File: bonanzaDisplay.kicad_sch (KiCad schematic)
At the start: 81 parts, among them J1 OLED-1.31-SSD1322, J15 SWD, J2 Conn_01x02, J5 Conn_01x10, J6 USB_C_Receptacle_USB2.0, SW1 TS-1088-AR02016, SW2 TS-1088-AR02016, SW3 SIQ-02FVS3, U1 RP2354A, U2 XC6206P302MR, U3 XC6206P282MR, U4 TPS62933DRLR, Y1 ABM8-272-T3

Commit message: updated version to v3. switch to 12P FPC
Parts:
- J5: footprint bonanzaDisplay:FPC-SMD_10P-P1.0_FGS-XJ-H2.0 -> bonanzaDisplay:FPC-SMD_12P-P1.00_FGS-XJ-H2.0; symbol bonanzaDisplay:FPC-SMD_10P-P1.0_FGS-XJ-H2.0 -> bonanzaDisplay:FPC-SMD_12P-P1.0_FGS-XJ-H2.0; LCSC C262756 -> C262757; PARTNO AFA01-S10FCA-00 -> AFA01-S12FCA-00
- TP22: value SCL -> TX
- TP23: value SDA -> RX
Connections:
- net GND: now also J5.13; no longer J5.11, J5.12
- net SWCLK: now also J5.12 (Pin_10)
- net DISP_SCL renamed DISP_TX
- net DISP_SDA renamed DISP_RX
- new net SWD-DISP: J5.11 (Pin_10)
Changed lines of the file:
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@@
 	(title_block
 		(title "bonanzaDisplay")
-		(date "2026-05-05")
-		(rev "v2")
+		(date "2026-10-01")
+		(rev "v3")
 		(company "bitaxeorg")
 		(comment 1 "OHL v2")
@@
 	(wire
 		(pts
+			(xy 71.12 134.62) (xy 57.15 134.62)
+		)
+		(stroke
+			(width 0)
+			(type default)
+		)
+	)
+	(wire
+		(pts
 			(xy 104.14 46.99) (xy 101.6 46.99)
 		)
@@
 	(wire
 		(pts
+			(xy 71.12 137.16) (xy 57.15 137.16)
+		)
+		(stroke
+			(width 0)
+			(type default)
+		)
+	)
+	(wire
+		(pts
 			(xy 218.44 58.42) (xy 223.52 58.42)
 		)
@@
 		)
 	)
+	(label "SWD-DISP"
+		(at 71.12 134.62 180)
+		(effects
+			(font
+				(size 1.27 1.27)
+			)
+			(justify right bottom)
+		)
+	)
 	(label "GND"
 		(at 256.54 227.33 0)
@@
 		)
 	)
+	(label "DISP_TX"
+		(at 71.12 127 180)
+		(effects
+			(font
+				(size 1.27 1.27)
+			)
+			(justify right bottom)
+		)
+	)
 	(label "SW_CCW"
 		(at 134.62 224.79 0)
@@
 		)
 	)
-	(label "DISP_SDA"
-		(at 247.65 144.78 180)
-		(effects
-			(font
-				(size 1.27 1.27)
-			)
-			(justify right bottom)
-		)
-	)
 	(label "GND"
 		(at 71.12 116.84 180)
@@
 		)
 	)
+	(label "DISP_RX"
+		(at 71.12 129.54 180)
+		(effects
+			(font
+				(size 1.27 1.27)
+			)
+			(justify right bottom)
+		)
+	)
 	(label "3V0"
 		(at 267.97 215.9 180)
@@
 		)
 	)
-	(label "DISP_SCL"
-		(at 71.12 127 180)
+	(label "DISP_RX"
+		(at 247.65 144.78 180)
+		(effects
+			(font
+				(size 1.27 1.27)
+			)
+			(justify right bottom)
+		)
+	)
+	(label "DISP_TX"
+		(at 247.65 147.32 180)
 		(effects
 			(font
@@
 		)
 	)
+	(label "SWCLK"
+		(at 71.12 137.16 180)
+		(effects
+			(font
+				(size 1.27 1.27)
+			)
+			(justify right bottom)
+		)
+	)
 	(label "E{slash}RD"
 		(at 320.04 170.18 0)
@@
 		)
 	)
-	(label "DISP_SCL"
-		(at 247.65 147.32 180)
-		(effects
-			(font
-				(size 1.27 1.27)
-			)
-			(justify right bottom)
-		)
-	)
 	(label "D1"
 		(at 320.04 165.1 0)
@@
 		)
 	)
-	(label "DISP_SDA"
-		(at 71.12 129.54 180)
-		(effects
-			(font
-				(size 1.27 1.27)
-			)
-			(justify right bottom)
-		)
-	)
 	(label "DISP_GPIO2"
 		(at 247.65 152.4 180)
@@
 			)
 		)
-		(property "Value" "SCL"
+		(property "Value" "TX"
 			(at 251.968 149.606 90)
 			(show_name no)
@@
 			)
 		)
-		(property "Value" "SDA"
+		(property "Value" "RX"
 			(at 263.398 147.066 90)
 			(show_name no)
@@
 	)
 	(symbol
-		(lib_id "bonanzaDisplay:FPC-SMD_10P-P1.0_FGS-XJ-H2.0")
+		(lib_id "bonanzaDisplay:FPC-SMD_12P-P1.0_FGS-XJ-H2.0")
 		(at 52.07 119.38 0)
 		(mirror y)
@@
 		(dnp no)
 		(property "Reference" "J5"
-			(at 52.07 134.874 0)
+			(at 52.07 106.68 0)
 			(show_name no)
 			(do_not_autoplace no)
@@
 		)
 		(property "Value" "Conn_01x10"
-			(at 51.816 136.652 0)
+			(at 51.816 139.954 0)
 			(show_name no)
 			(do_not_autoplace no)
@@
 			)
 		)
-		(property "Footprint" "bonanzaDisplay:FPC-SMD_10P-P1.0_FGS-XJ-H2.0"
-			(at 52.07 119.38 0)
+		(property "Footprint" "bonanzaDisplay:FPC-SMD_12P-P1.00_FGS-XJ-H2.0"
+			(at 52.07 143.002 0)
 			(hide yes)
 			(show_name no)
@@
 		)
 		(property "Datasheet" "https://www.lcsc.com/datasheet/C262756.pdf"
-			(at 52.07 119.38 0)
+			(at 52.07 143.002 0)
 			(hide yes)
 			(show_name no)
@@
 			)
 		)
-		(property "PARTNO" "AFA01-S10FCA-00"
-			(at 52.07 119.38 0)
+		(property "PARTNO" "AFA01-S12FCA-00"
+			(at 52.07 143.002 0)
 			(hide yes)
 			(show_name no)
@@
 			)
 		)
-		(property "LCSC" "C262756"
-			(at 52.07 119.38 0)
+		(property "LCSC" "C262757"
+			(at 51.562 145.034 0)
 			(hide yes)
 			(show_name no)
@@
 		(pin "11"
 		)
+		(pin "13"
+		)
+		(pin "14"
+		)
 		(instances

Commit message: rough placements and critical routing done
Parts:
- removed J6: USB_C_Receptacle_USB2.0, bonanzaDisplay:USB_C_Receptacle_GCT_USB4105-xx-A, symbol bonanzaDisplay:USB_C_Receptacle_USB2.0
- added J6: TYPE-C-31-M-12, bonanzaDisplay:USB-C_SMD-TYPE-C-31-M-12_1, symbol bitaxe:TYPE-C-31-M-12
- added TP64: VBUS, bonanzaDisplay:TestPoint_Pad_D1.0mm, symbol Connector:TestPoint
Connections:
- net SWD-DISP is gone; now on net SWD: J5.11 (Pin_10)
- net GND: now also J6.1 (SHIELD), J6.2 (EH), J6.3 (EH), J6.4 (EH), J6.A1B12 (GND), J6.B1A12 (GND)
- net USB_DN: now also J6.A7 (DN1), J6.B7 (DN2)
- net USB_DP: now also J6.A6 (DP1), J6.B6 (DP2)
- net at R4.2: now also J6.B5 (CC2)
- net at R2.2: now also J6.A5 (CC1)
- new net: J6.A4B9 (VBUS), J6.B4A9 (VBUS), TP64.1
- no-connect marks 21 -> 20
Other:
- moved on the sheet: R2, R4

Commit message: finished routing, DRC and ERC pass
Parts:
- removed H1, H2, H3, H4: MountingHole_Pad, MountingHole:MountingHole_3.2mm_M3, symbol Mechanical:MountingHole
- J6: symbol bitaxe:TYPE-C-31-M-12 -> bonanzaDisplay:TYPE-C-31-M-12
- SW1, SW2: symbol bitaxe:GT-TC029B-H025-L1N -> bonanzaDisplay:GT-TC029B-H025-L1N
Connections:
- net GND: now also J5.14
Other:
- note added: "Display Ref Voltage Regulators"
- moved on the sheet: C38, C39, C40, TP15, TP16, TP18, U2, U3

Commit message: add jlcpcb offsets
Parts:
- J1: FT Position Offset (none) -> 0,-3.4
- U2, U3, U4: FT Rotation Offset (none) -> -180
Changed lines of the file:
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@@
 			)
 		)
+		(property "FT Rotation Offset" "-180"
+			(at 241.3 219.71 0)
+			(hide yes)
+			(show_name no)
+			(do_not_autoplace no)
+			(effects
+				(font
+					(size 1.27 1.27)
+				)
+			)
+		)
 		(pin "3"
 		)
@@
 			)
 		)
+		(property "FT Rotation Offset" "-180"
+			(at 78.74 49.53 0)
+			(hide yes)
+			(show_name no)
+			(do_not_autoplace no)
+			(effects
+				(font
+					(size 1.27 1.27)
+				)
+			)
+		)
 		(pin "4"
 		)
@@
 			)
 		)
+		(property "FT Rotation Offset" "-180"
+			(at 241.3 243.84 0)
+			(hide yes)
+			(show_name no)
+			(do_not_autoplace no)
+			(effects
+				(font
+					(size 1.27 1.27)
+				)
+			)
+		)
 		(pin "3"
 		)
@@
 			(at 336.55 172.72 0)
 			(hide yes)
+			(show_name no)
+			(do_not_autoplace no)
+			(effects
+				(font
+					(size 1.27 1.27)
+				)
+			)
+		)
+		(property "FT Position Offset" "0,-3.4"
+			(at 336.55 172.72 0)
+			(hide yes)

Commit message: removed the OLED accessory voltage regulators -- we should be good with 3.3V. addressed VCOMH bypass cap voltage rating.
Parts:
- removed C38, C39, C40: 1uF, Capacitor_SMD:C_0402_1005Metric, symbol Device:C_Small
- removed R39: 4.7k, Resistor_SMD:R_0402_1005Metric, symbol Device:R_Small_US
- removed TP15: 3V0, bonanzaDisplay:TestPoint_Pad_D1.0mm, symbol Connector:TestPoint
- removed TP16: 2V8, bonanzaDisplay:TestPoint_Pad_D1.0mm, symbol Connector:TestPoint
- removed TP17: 1V1, bonanzaDisplay:TestPoint_Pad_D1.0mm, symbol Connector:TestPoint
- removed TP18: GND, bonanzaDisplay:TestPoint_Pad_D1.0mm, symbol Connector:TestPoint
- removed U2: XC6206P302MR, Package_TO_SOT_SMD:SOT-23, symbol bonanzaDisplay:XC6206
- removed U3: XC6206P282MR, Package_TO_SOT_SMD:SOT-23, symbol bonanzaDisplay:XC6206
- C26: footprint Capacitor_SMD:C_0402_1005Metric -> Capacitor_SMD:C_1206_3216Metric; Dielectric (none) -> X7R; LCSC C23733 -> C51205; Manufacturer Murata Electronics -> Samsung Electro-Mechanics; PARTNO CL05A475KP5NRNC -> CL31B475KBHNNNE; Tolerance (none) -> ±10%; Voltage (none) -> 50V
- J1: value OLED-1.31-SSD1322 -> OLED-3.12-SSD1322
- U1: private KLC_S4.2_VREG_LX -> KLC_S4.2_DVDD; private_1 (none) -> KLC_S4.2_VREG_LX
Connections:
- net 2V8 is gone; now on net 3V3: J1.24 (VDDIO)
- net 3V0 is gone; now on net 3V3: C19.1, C21.1, J1.17 (BS1)
- net 3V3: now also J1.26 (VCI)
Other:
- note added: "EA W256064-XALG 3.12" OLED Module"
- note added: "OLED logic supply: shared MCU 3V3 VCI, VDDIO and BS1 use the same rail. VDD (pin 25): internal regulator; C22 only."
- note removed: "Display Ref Voltage Regulators"

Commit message: Correct RP2354A crystal BOM and load capacitors (H3)
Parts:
- C16, C17: value 10pF -> 15pF; Dielectric (none) -> C0G; LCSC C32949 -> C1548; Manufacturer Murata Electronics -> FH (Guangdong Fenghua Advanced Tech); PARTNO (none) -> 0402CG150J500NT; Tolerance (none) -> ±5%; Voltage (none) -> 50V
- Y1: LCSC C9002 -> C20625731; Manufacturer Abracon -> Abracon LLC
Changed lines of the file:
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@@
 			)
 		)
-		(property "Datasheet" ""
+		(property "Datasheet" "https://abracon.com/datasheets/ABM8-272-T3.pdf"
 			(at 140.97 152.4 0)
 			(hide yes)
@@
 			)
 		)
-		(property "Manufacturer" "Abracon "
+		(property "Manufacturer" "Abracon LLC"
 			(at 140.97 152.4 0)
 			(hide yes)
@@
 			)
 		)
-		(property "LCSC" "C9002"
+		(property "LCSC" "C20625731"
 			(at 74.93 139.7 0)
 			(hide yes)
@@
 			)
 		)
-		(property "Value" "10pF"
+		(property "Value" "15pF"
 			(at 129.54 159.258 90)
 			(show_name no)
@@
 			)
 		)
-		(property "Datasheet" ""
+		(property "Datasheet" "https://www.lcsc.com/datasheet/lcsc_datasheet_2304140030_FH--Guangdong-Fenghua-Advanced-Tech-0402CG150J500NT_C1548.pdf"
 			(at 135.89 157.48 0)
 			(hide yes)
@@
 			)
 		)
-		(property "Manufacturer" "Murata Electronics"
+		(property "Manufacturer" "FH (Guangdong Fenghua Advanced Tech)"
 			(at 135.89 157.48 0)
 			(hide yes)
@@
 			)
 		)
-		(property "LCSC" "C32949"
+		(property "LCSC" "C1548"
 			(at 135.89 157.48 0)
 			(hide yes)
@@
 			)
 		)
-		(property "PARTNO" ""
+		(property "PARTNO" "0402CG150J500NT"
 			(at 135.89 157.48 90)
 			(hide yes)
@@
 			)
 		)
-	)
+		(property "Dielectric" "C0G"
+			(at 135.89 157.48 0)
+			(hide yes)
+			(effects
+				(font
+					(size 1.27 1.27)
+				)
+			)
+		)
+		(property "Tolerance" "±5%"
+			(at 135.89 157.48 0)
+			(hide yes)
+			(effects
+				(font
+					(size 1.27 1.27)
+				)
+			)
+		)
+		(property "Voltage" "50V"
+			(at 135.89 157.48 0)
+			(hide yes)
+			(effects
+				(font
+					(size 1.27 1.27)
+				)
+			)
+		))
 	(symbol
 		(lib_id "Device:R_Small_US")
@@
 			)
 		)
-		(property "Value" "10pF"
+		(property "Value" "15pF"
 			(at 129.794 148.59 90)
 			(show_name no)
@@
 			)
 		)
-		(property "Datasheet" ""
+		(property "Datasheet" "https://www.lcsc.com/datasheet/lcsc_datasheet_2304140030_FH--Guangdong-Fenghua-Advanced-Tech-0402CG150J500NT_C1548.pdf"
 			(at 135.89 147.32 0)
 			(hide yes)
@@
 			)
 		)
-		(property "Manufacturer" "Murata Electronics"
+		(property "Manufacturer" "FH (Guangdong Fenghua Advanced Tech)"
 			(at 135.89 147.32 0)
 			(hide yes)
@@
 			)
 		)
-		(property "LCSC" "C32949"
+		(property "LCSC" "C1548"
 			(at 135.89 147.32 0)
 			(hide yes)
@@
 			)
 		)
-		(property "PARTNO" ""
+		(property "PARTNO" "0402CG150J500NT"
 			(at 135.89 147.32 90)
 			(hide yes)
@@
 			)
 		)
-	)
+		(property "Dielectric" "C0G"
+			(at 135.89 147.32 0)
+			(hide yes)
+			(effects
+				(font
+					(size 1.27 1.27)
+				)
+			)
+		)
+		(property "Tolerance" "±5%"
+			(at 135.89 147.32 0)
+			(hide yes)
+			(effects
+				(font
+					(size 1.27 1.27)
+				)
+			)
+		)
+		(property "Voltage" "50V"
+			(at 135.89 147.32 0)
+			(hide yes)
+			(effects
+				(font
+					(size 1.27 1.27)
+				)
+			)
+		))
 	(symbol
 		(lib_id "bonanzaDisplay:FPC-SMD_12P-P1.0_FGS-XJ-H2.0")

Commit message: Sync reviewed v3.1 PCB fixes and protect BOOT chip-select
Add R40 (1k, 0402, C11702) between QSPI_SS and SW2, including the
reviewed via placement on its switch-side pad and refreshed zone fills.

Include the manually synchronized OLED power, bypass capacitor and
crystal changes, corrected C16/C17 MPNs, connector datasheet links,
and the v3.1 project revision metadata.

Validation: zero DRC violations, zero unconnected items, and zero
schematic/PCB parity mismatches. All 19 existing ERC findings are
unchanged. Hardware BOOTSEL testing and assembly-process checks remain
open.

Refs #3, #4, #5, #6, #8, #9, #12, #16
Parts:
- added R40: 1k, Resistor_SMD:R_0402_1005Metric, symbol Device:R_Small_US
- J5: value Conn_01x10 -> Conn_01x12
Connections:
- net at SW2.1: now also R40.2; no longer U1.60 (~{QSPI_SS})
- new net: R40.1, U1.60 (~{QSPI_SS})

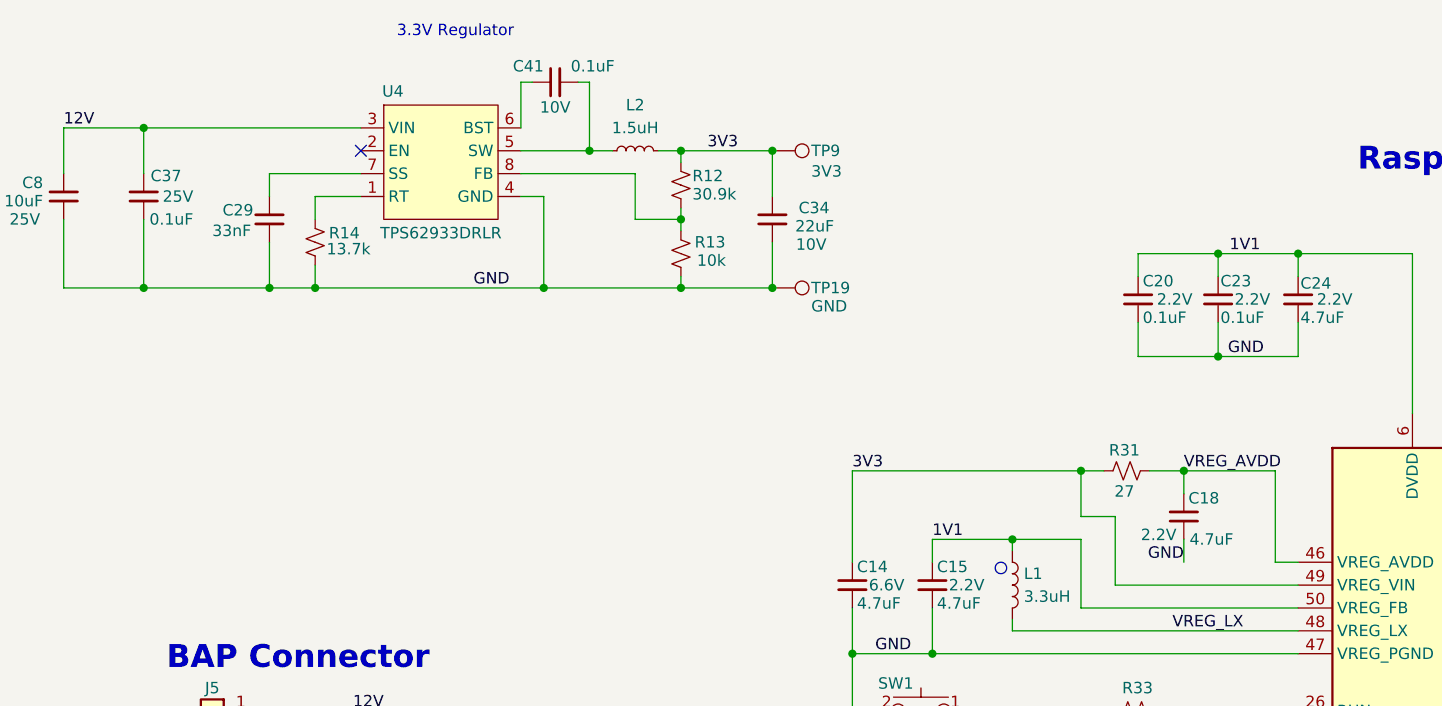
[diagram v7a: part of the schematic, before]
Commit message: Apply reviewed fabrication rules and ERC model fixes
Configure JLCPCB six-layer DFM rules and correct via drills, USB VBUS clearances, and silkscreen. Document filled-and-capped via requirements and remaining supplier preview checks.

Correct project symbol pin types and add verified power-source assertions without changing circuit connectivity. ERC, DRC, unconnected-item and schematic parity checks pass.

Refs #11, #12, #15
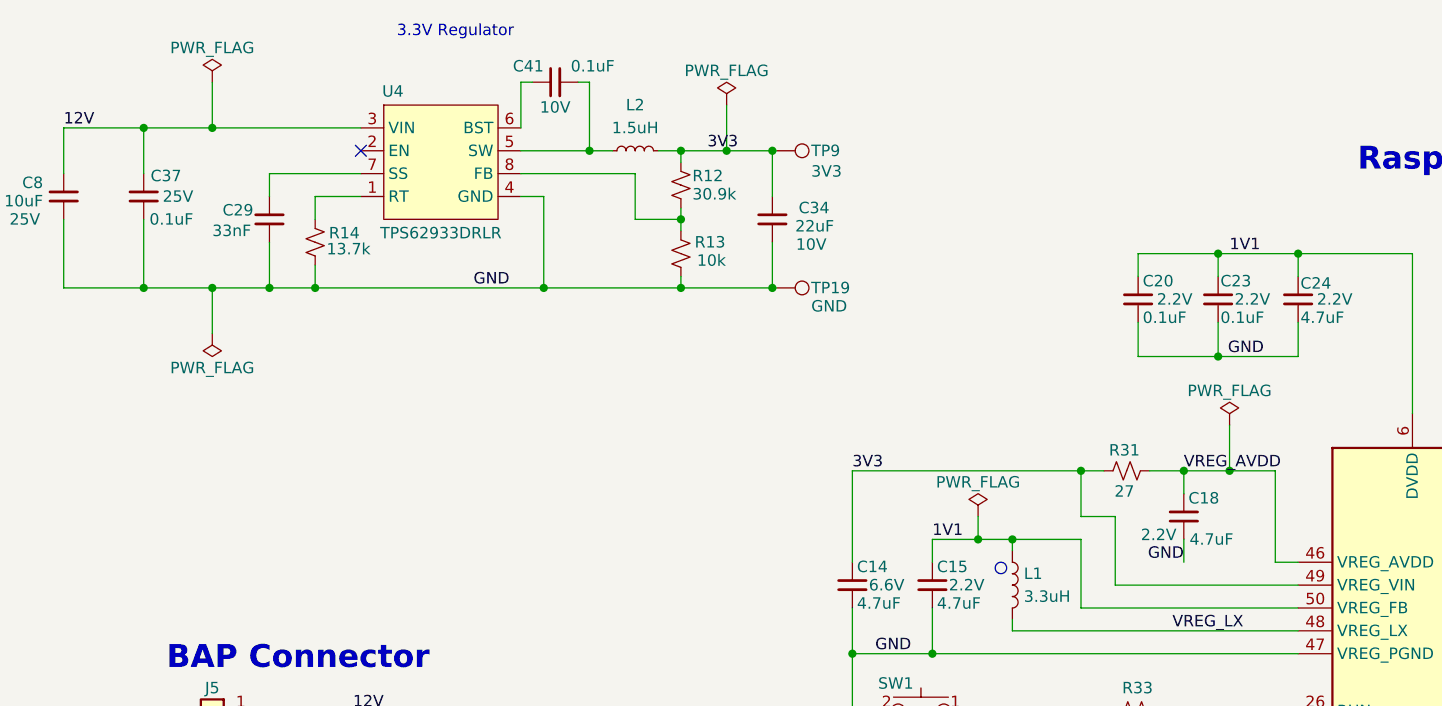
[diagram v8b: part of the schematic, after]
